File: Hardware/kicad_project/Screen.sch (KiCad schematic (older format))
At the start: 10 parts

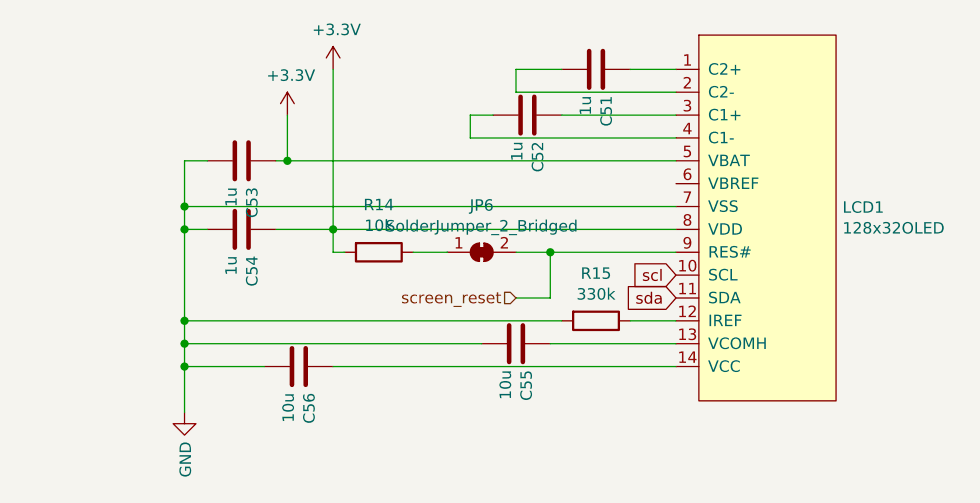
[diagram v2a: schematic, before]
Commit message: new hardware rev
reworked power system
added amp
new LDOS (less dropout)
dedicated LDO for audio system
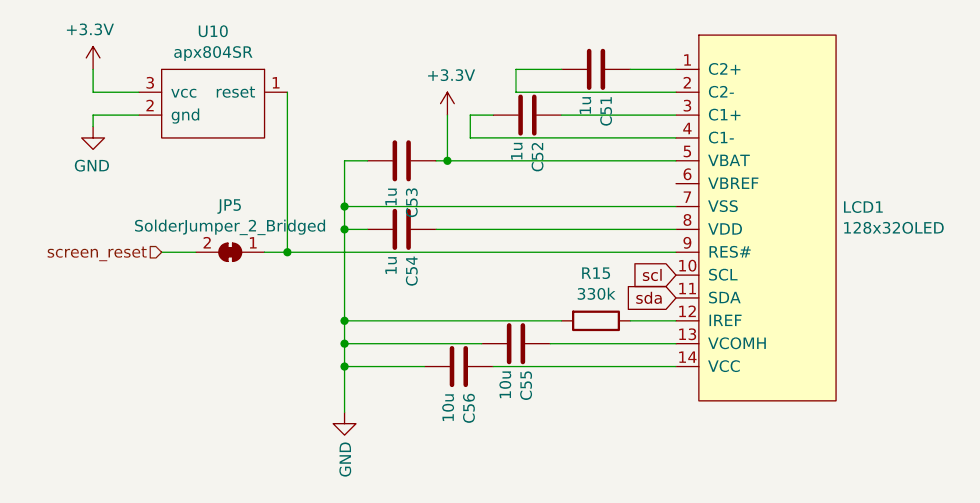
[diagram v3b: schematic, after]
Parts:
- removed JP6: SolderJumper_2_Bridged, Jumper:SolderJumper-2_P1.3mm_Bridged_RoundedPad1.0x1.5mm, symbol Jumper:SolderJumper_2_Bridged
- removed R14: 10k, Resistors_SMD:R_0402_NoSilk, symbol Device:R
- added JP5: SolderJumper_2_Bridged, Jumper:SolderJumper-2_P1.3mm_Bridged_Pad1.0x1.5mm, symbol Jumper:SolderJumper_2_Bridged
- added U10: apx804SR, TO_SOT_Packages_SMD:SOT-23, symbol customLibrary:apx804SR
- LCD1: checked (none) -> 1
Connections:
- net +3V3: now also U10.3 (vcc); no longer C54.1, LCD1.8 (VDD)
- net GND: now also U10.2 (gnd)
- net screen_reset: now also JP5.2 (B); no longer LCD1.9 (RES#)
- new net: JP5.1 (A), LCD1.9 (RES#), U10.1 (reset)
- new net: C54.1, LCD1.8 (VDD)
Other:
- moved on the sheet: C53, C54, C56
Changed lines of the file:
@@
 F 2 "RandomJunk:oled_ssd1306_14pin_91" H 6550 3800 50  0001 C CNN
 F 3 "" H 6550 3800 50  0001 C CNN
+F 4 "1" H 6500 3750 50  0001 C CNN "checked"
 	1    6500 3750
 	1    0    0    -1
@@
 L Device:C C53
 U 1 1 6364F39B
-P 4200 3500
-F 0 "C53" H 4315 3546 50  0000 L CNN
-F 1 "1u" H 4315 3455 50  0000 L CNN
-F 2 "Capacitors_SMD:C_0402_NoSilk" H 4238 3350 50  0001 C CNN
-F 3 "~" H 4200 3500 50  0001 C CNN
-F 4 "C52923" H 4200 3500 50  0001 C CNN "LCSC"
-	1    4200 3500
+P 4900 3500
+F 0 "C53" H 5015 3546 50  0000 L CNN
+F 1 "1u" H 5015 3455 50  0000 L CNN
+F 2 "Capacitors_SMD:C_0402_NoSilk" H 4938 3350 50  0001 C CNN
+F 3 "~" H 4900 3500 50  0001 C CNN
+F 4 "C52923" H 4900 3500 50  0001 C CNN "LCSC"
+	1    4900 3500
 	0    1    1    0
 $EndComp
@@
 L Device:C C54
 U 1 1 6364F3A2
-P 4200 3800
-F 0 "C54" H 4315 3846 50  0000 L CNN
-F 1 "1u" H 4315 3755 50  0000 L CNN
-F 2 "Capacitors_SMD:C_0402_NoSilk" H 4238 3650 50  0001 C CNN
-F 3 "~" H 4200 3800 50  0001 C CNN
-F 4 "C52923" H 4200 3800 50  0001 C CNN "LCSC"
-	1    4200 3800
+P 4900 3800
+F 0 "C54" H 5015 3846 50  0000 L CNN
+F 1 "1u" H 5015 3755 50  0000 L CNN
+F 2 "Capacitors_SMD:C_0402_NoSilk" H 4938 3650 50  0001 C CNN
+F 3 "~" H 4900 3800 50  0001 C CNN
+F 4 "C52923" H 4900 3800 50  0001 C CNN "LCSC"
+	1    4900 3800
 	0    1    1    0
 $EndComp
@@
 L power:+3.3V #PWR039
 U 1 1 6364F3A8
-P 4400 3300
-F 0 "#PWR039" H 4400 3150 50  0001 C CNN
-F 1 "+3.3V" H 4415 3473 50  0000 C CNN
-F 2 "" H 4400 3300 50  0001 C CNN
-F 3 "" H 4400 3300 50  0001 C CNN
-	1    4400 3300
+P 5100 3300
+F 0 "#PWR039" H 5100 3150 50  0001 C CNN
+F 1 "+3.3V" H 5115 3473 50  0000 C CNN
+F 2 "" H 5100 3300 50  0001 C CNN
+F 3 "" H 5100 3300 50  0001 C CNN
+	1    5100 3300
 	1    0    0    -1
 $EndComp
-$Comp
-L power:+3.3V #PWR038
-U 1 1 6364F3AE
-P 4600 3100
-F 0 "#PWR038" H 4600 2950 50  0001 C CNN
-F 1 "+3.3V" H 4615 3273 50  0000 C CNN
-F 2 "" H 4600 3100 50  0001 C CNN
-F 3 "" H 4600 3100 50  0001 C CNN
-	1    4600 3100
-	1    0    0    -1
-$EndComp
-Wire Wire Line
-	6100 3500 4400 3500
-Wire Wire Line
-	4400 3300 4400 3500
-Connection ~ 4400 3500
-Wire Wire Line
-	4400 3500 4350 3500
-Wire Wire Line
-	4350 3800 4600 3800
-Connection ~ 4600 3800
-Wire Wire Line
-	4600 3800 6100 3800
+Wire Wire Line
+	6100 3500 5100 3500
+Wire Wire Line
+	5100 3300 5100 3500
+Connection ~ 5100 3500
+Wire Wire Line
+	5100 3500 5050 3500
 $Comp
 L power:GND #PWR040
 U 1 1 6364F3BB
-P 3950 4600
-F 0 "#PWR040" H 3950 4350 50  0001 C CNN
-F 1 "GND" V 3955 4472 50  0000 R CNN
-F 2 "" H 3950 4600 50  0001 C CNN
-F 3 "" H 3950 4600 50  0001 C CNN
-	1    3950 4600
+P 4650 4600
+F 0 "#PWR040" H 4650 4350 50  0001 C CNN
+F 1 "GND" V 4655 4472 50  0000 R CNN
+F 2 "" H 4650 4600 50  0001 C CNN
+F 3 "" H 4650 4600 50  0001 C CNN
+	1    4650 4600
 	1    0    0    -1
 $EndComp
@@
 L Device:C C56
 U 1 1 6364F3C2
-P 4450 4400
-F 0 "C56" H 4565 4446 50  0000 L CNN
-F 1 "10u" H 4565 4355 50  0000 L CNN
-F 2 "Capacitors_SMD:C_0402_NoSilk" H 4488 4250 50  0001 C CNN
-F 3 "~" H 4450 4400 50  0001 C CNN
-F 4 "C15525" H 4450 4400 50  0001 C CNN "LCSC"
-	1    4450 4400
+P 5150 4400
+F 0 "C56" H 5265 4446 50  0000 L CNN
+F 1 "10u" H 5265 4355 50  0000 L CNN
+F 2 "Capacitors_SMD:C_0402_NoSilk" H 5188 4250 50  0001 C CNN
+F 3 "~" H 5150 4400 50  0001 C CNN
+F 4 "C15525" H 5150 4400 50  0001 C CNN "LCSC"
+	1    5150 4400
 	0    1    1    0
 $EndComp
@@
 	6100 4200 5900 4200
 Wire Wire Line
-	5600 4200 3950 4200
-Wire Wire Line
-	3950 4200 3950 4300
+	5600 4200 4650 4200
+Wire Wire Line
+	4650 4200 4650 4300
 Wire Wire Line
 	6100 4300 5550 4300
 Wire Wire Line
-	5250 4300 3950 4300
-Connection ~ 3950 4300
-Wire Wire Line
-	3950 4300 3950 4400
-Wire Wire Line
-	4300 4400 3950 4400
-Connection ~ 3950 4400
-Wire Wire Line
-	3950 4400 3950 4600
-Wire Wire Line
-	4600 4400 6100 4400
-Wire Wire Line
-	4050 3800 3950 3800
-Connection ~ 3950 4200
-Wire Wire Line
-	4050 3500 3950 3500
-Wire Wire Line
-	3950 3500 3950 3700
-Connection ~ 3950 3800
-Wire Wire Line
-	3950 3800 3950 4200
-Wire Wire Line
-	3950 3700 6100 3700
-Connection ~ 3950 3700
-Wire Wire Line
-	3950 3700 3950 3800
-$Comp
-L Device:R R14
-U 1 1 6364F3E9
-P 4800 3900
-F 0 "R14" V 4593 3900 50  0000 C CNN
-F 1 "10k" V 4684 3900 50  0000 C CNN
-F 2 "Resistors_SMD:R_0402_NoSilk" V 4730 3900 50  0001 C CNN
-F 3 "~" H 4800 3900 50  0001 C CNN
-F 4 "C25744" H 4800 3900 50  0001 C CNN "LCSC"
-	1    4800 3900
-	0    1    1    0
-$EndComp
-Wire Wire Line
-	6100 3900 5550 3900
-Wire Wire Line
-	4600 3100 4600 3800
-Wire Wire Line
-	4650 3900 4600 3900
-Wire Wire Line
-	4600 3900 4600 3800
-Text HLabel 5400 4100 0    50   Input ~ 0
+	5250 4300 4650 4300
+Connection ~ 4650 4300
+Wire Wire Line
+	4650 4300 4650 4400
+Wire Wire Line
+	5000 4400 4650 4400
+Connection ~ 4650 4400
+Wire Wire Line
+	4650 4400 4650 4600
+Wire Wire Line
+	5300 4400 6100 4400
+Wire Wire Line
+	4750 3800 4650 3800
+Connection ~ 4650 4200
+Wire Wire Line
+	4750 3500 4650 3500
+Wire Wire Line
+	4650 3500 4650 3700
+Connection ~ 4650 3800
+Wire Wire Line
+	4650 3800 4650 4200
+Wire Wire Line
+	4650 3700 6100 3700
+Connection ~ 4650 3700
+Wire Wire Line
+	4650 3700 4650 3800
+Text HLabel 3850 3900 0    50   Input ~ 0
 screen_reset
 $Comp
-L Jumper:SolderJumper_2_Bridged JP6
-U 1 1 61E0FF09
-P 5250 3900
-F 0 "JP6" H 5250 4105 50  0000 C CNN
-F 1 "SolderJumper_2_Bridged" H 5250 4014 50  0000 C CNN
-F 2 "Jumper:SolderJumper-2_P1.3mm_Bridged_RoundedPad1.0x1.5mm" H 5250 3900 50  0001 C CNN
-F 3 "~" H 5250 3900 50  0001 C CNN
-	1    5250 3900
-	1    0    0    -1
-$EndComp
-Wire Wire Line
-	5100 3900 4950 3900
-Wire Wire Line
-	5400 4100 5550 4100
-Wire Wire Line
-	5550 4100 5550 3900
-Connection ~ 5550 3900
-Wire Wire Line
-	5550 3900 5400 3900
+L Jumper:SolderJumper_2_Bridged JP?
+U 1 1 620F1C3B
+P 4150 3900
+AR Path="/62E6C628/620F1C3B" Ref="JP?"  Part="1"
+AR Path="/63637E58/620F1C3B" Ref="JP5"  Part="1"
+F 0 "JP5" H 4150 4105 50  0000 C CNN
+F 1 "SolderJumper_2_Bridged" H 4150 4014 50  0000 C CNN
+F 2 "Jumper:SolderJumper-2_P1.3mm_Bridged_Pad1.0x1.5mm" H 4150 3900 50  0001 C CNN
+F 3 "~" H 4150 3900 50  0001 C CNN
+F 4 "1" H 4150 3900 50  0001 C CNN "checked"
+	1    4150 3900
+	-1   0    0    -1
+$EndComp
+Wire Wire Line
+	3850 3900 4000 3900
+Wire Wire Line
+	4400 3200 4400 3900
+Connection ~ 4400 3900
+Wire Wire Line
+	4400 3900 4300 3900
+$Comp
+L customLibrary:apx804SR U?
+U 1 1 620F1C46
+P 4050 3250
+AR Path="/62E6C628/620F1C46" Ref="U?"  Part="1"
+AR Path="/63637E58/620F1C46" Ref="U10"  Part="1"
+F 0 "U10" H 4025 3565 50  0000 C CNN
+F 1 "apx804SR" H 4025 3474 50  0000 C CNN
+F 2 "TO_SOT_Packages_SMD:SOT-23" H 4050 3550 50  0001 C CNN
+F 3 "" H 4050 3550 50  0001 C CNN
+	1    4050 3250
+	-1   0    0    -1
+$EndComp
+Wire Wire Line
+	3550 3200 3550 3100
+Wire Wire Line
+	3750 3200 3550 3200
+Wire Wire Line
+	3550 3300 3550 3350
+Wire Wire Line
+	3750 3300 3550 3300
+$Comp
+L power:GND #PWR?
+U 1 1 620F1C50
+P 3550 3350
+AR Path="/620F1C50" Ref="#PWR?"  Part="1"
+AR Path="/62E6C628/620F1C50" Ref="#PWR?"  Part="1"
+AR Path="/63637E58/620F1C50" Ref="#PWR0118"  Part="1"
+F 0 "#PWR0118" H 3550 3100 50  0001 C CNN
+F 1 "GND" H 3555 3177 50  0000 C CNN
+F 2 "" H 3550 3350 50  0001 C CNN
+F 3 "" H 3550 3350 50  0001 C CNN
+	1    3550 3350
+	-1   0    0    -1
+$EndComp
+$Comp
+L power:+3.3V #PWR?
+U 1 1 620F1C56
+P 3550 3100
+AR Path="/620F1C56" Ref="#PWR?"  Part="1"
+AR Path="/62E6C628/620F1C56" Ref="#PWR?"  Part="1"
+AR Path="/63637E58/620F1C56" Ref="#PWR0119"  Part="1"
+F 0 "#PWR0119" H 3550 2950 50  0001 C CNN
+F 1 "+3.3V" H 3565 3273 50  0000 C CNN
+F 2 "" H 3550 3100 50  0001 C CNN
+F 3 "" H 3550 3100 50  0001 C CNN
+	1    3550 3100
+	-1   0    0    -1
+$EndComp
+Wire Wire Line
+	5050 3800 6100 3800
+Wire Wire Line
+	4400 3900 6100 3900
 $EndSCHEMATC
